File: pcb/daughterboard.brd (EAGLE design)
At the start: 28 x 24 mm, 21 parts, among them IC3 STM32F042F4, SW1 324_SW324_SWITCH_FOOT_HOLE, SW2 324_SW324_SWITCH_FOOT_HOLE, SW3 324_SW, SW4 324_SW, SW5 324_SW324_SWITCH_FOOT_HOLE, SW6 324_SW324_SWITCH_FOOT_HOLE, U2 USBC_16P, U4 XC6206_DEV

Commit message: working on new version
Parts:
- C4: value 1uF -> 100nF
- JP1: device pinhead:2X04 -> pinhead:2X03
- moved C4 5.09 mm to (2.16, 17.9)
- moved JP1 0.55 mm to (10.0, 20.7)
- moved U2 0.38 mm to (5.08, 3.81)
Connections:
- new net N$1: IC3.14, JP1.4
- net +3V3: no longer LED2.A
- net +5V: now also JP1.1
- net GND: now also JP1.2
- net USB_DN: now also IC3.17
- net USB_DP: now also IC3.18
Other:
- board size 28 x 24 mm -> 29 x 24 mm
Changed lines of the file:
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@@
 <setting verticaltext="up"/>
 </settings>
-<grid distance="5" unitdist="mil" unit="mil" style="lines" multiple="1" display="no" altdistance="1" altunitdist="mil" altunit="mil"/>
+<grid distance="5" unitdist="mil" unit="mm" style="lines" multiple="1" display="no" altdistance="1" altunitdist="mil" altunit="mil"/>
 <layers>
 <layer number="1" name="Top" color="4" fill="1" visible="yes" active="yes"/>
@@
 <layer number="43" name="vRestrict" color="2" fill="10" visible="no" active="yes"/>
 <layer number="44" name="Drills" color="7" fill="1" visible="no" active="yes"/>
-<layer number="45" name="Holes" color="7" fill="1" visible="no" active="yes"/>
+<layer number="45" name="Holes" color="7" fill="1" visible="yes" active="yes"/>
 <layer number="46" name="Milling" color="3" fill="1" visible="yes" active="yes"/>
 <layer number="47" name="Measures" color="7" fill="1" visible="no" active="yes"/>
@@
 <plain>
 <wire x1="0" y1="24" x2="0" y2="0" width="0" layer="20"/>
-<wire x1="0" y1="0" x2="28" y2="0" width="0" layer="20"/>
-<wire x1="28" y1="0" x2="28" y2="24" width="0" layer="20"/>
-<wire x1="28" y1="24" x2="0" y2="24" width="0" layer="20"/>
+<wire x1="0" y1="0" x2="29" y2="0" width="0" layer="20"/>
+<wire x1="29" y1="0" x2="29" y2="24" width="0" layer="20"/>
+<wire x1="29" y1="24" x2="0" y2="24" width="0" layer="20"/>
 <text x="69.342" y="33.782" size="0.889" layer="25">SCL</text>
 <text x="66.675" y="33.782" size="0.889" layer="25">SDA</text>
@@
 <text x="68.975" y="21.677" size="1.6764" layer="26" rot="MR180" align="center">git.io/bob_rewind</text>
 <text x="64.135" y="33.782" size="0.889" layer="25">VCC</text>
-<hole x="14" y="2" drill="3"/>
-<circle x="14" y="2" radius="2.6" width="0" layer="41"/>
+<hole x="13" y="2" drill="3"/>
+<circle x="13" y="2" radius="2.6" width="0" layer="41"/>
 <text x="39.925" y="0.68" size="1.778" layer="25" rot="R180" align="center">MOMENTORY
 PSW</text>
@@
 </autorouter>
 <elements>
-<element name="U2" library="my_usbc_16p" package="USBC_16P_FOOT" value="USBC_16P" x="5.461" y="3.81" smashed="yes"/>
+<element name="U2" library="my_usbc_16p" package="USBC_16P_FOOT" value="USBC_16P" x="5.08" y="3.81" smashed="yes"/>
 <element name="R1" library="joyAnalog" package="0805" value="5.1K" x="8.89" y="10.668" smashed="yes" rot="R90">
 <attribute name="NAME" x="28.4218" y="-46.1264" size="0.8128" layer="25" rot="R90"/>
@@
 </element>
 <element name="IC3" library="tx" package="TSSOP20" value="STM32F042F4" x="14.464" y="13.304" smashed="yes" rot="R90"/>
-<element name="C4" library="clock" package="0805@1" value="1uF" x="1.778" y="12.827" smashed="yes">
-<attribute name="NAME" x="53.1622" y="31.5341" size="0.8128" layer="25"/>
+<element name="C4" library="clock" package="0805@1" value="100nF" x="2.159" y="17.907" smashed="yes">
+<attribute name="NAME" x="53.5432" y="36.6141" size="0.8128" layer="25"/>
 </element>
 <element name="SW3" library="3pos_slide_switch_centered" package="342_SWICH_FOOT" value="324_SW" x="21.082" y="9.271" smashed="yes" rot="R90"/>
@@
 <attribute name="NAME" x="62.5564" y="35.0355" size="0.8128" layer="25"/>
 </element>
-<element name="JP1" library="pinhead" library_urn="urn:adsk.eagle:library:325" package="2X04" package3d_urn="urn:adsk.eagle:package:22461/2" value="" x="9.779" y="21.209" smashed="yes">
-<attribute name="POPULARITY" value="47" x="9.779" y="21.209" size="1.778" layer="27" display="off"/>
-<attribute name="VALUE" x="5.969" y="16.764" size="1.27" layer="27"/>
+<element name="JP1" library="pinhead" library_urn="urn:adsk.eagle:library:325" package="2X03" package3d_urn="urn:adsk.eagle:package:22462/2" value="" x="10" y="20.71" locked="yes" smashed="yes">
+<attribute name="POPULARITY" value="62" x="10" y="20.71" locked="yes" size="1.778" layer="27" display="off"/>
+<attribute name="VALUE" x="6.19" y="16.265" locked="yes" size="1.27" layer="27"/>
 </element>
 <element name="SW2" library="3pos_slide_switch" package="342_SWICH_FOOT_HOLE" value="324_SW324_SWITCH_FOOT_HOLE" x="26.289" y="11.43" smashed="yes" rot="R90"/>
@@
 <contactref element="U4" pad="1"/>
 <contactref element="C2" pad="1"/>
-<wire x1="16.038" y1="18.0594" x2="9.7934" y2="27.8638" width="0" layer="19" extent="1-1"/>
+<contactref element="JP1" pad="2"/>
+<wire x1="7.46" y1="21.98" x2="9.7934" y2="27.8638" width="0" layer="19" extent="1-1"/>
 </signal>
 <signal name="+3V3">
@@
 <contactref element="IC3" pad="5"/>
 <contactref element="C4" pad="2"/>
-<contactref element="LED2" pad="A"/>
 <contactref element="SW4" pad="P$1"/>
 <contactref element="SW4" pad="P$4"/>
@@
 <wire x1="8.8392" y1="13.324" x2="11.5462" y2="12.979" width="0" layer="19" extent="1-1"/>
 <wire x1="4.638" y1="12.43" x2="8.8392" y2="13.324" width="0" layer="19" extent="1-1"/>
-<wire x1="2.678" y1="12.827" x2="4.638" y2="12.43" width="0" layer="19" extent="1-1"/>
-<wire x1="3.315" y1="28.032" x2="2.678" y2="12.827" width="0" layer="19" extent="1-1"/>
+<wire x1="3.059" y1="17.907" x2="4.638" y2="12.43" width="0" layer="19" extent="1-1"/>
 </signal>
 <signal name="USB_DP">
 <contactref element="U2" pad="A6"/>
 <contactref element="U2" pad="B6"/>
-<wire x1="6.211" y1="7.6575" x2="5.211" y2="7.6575" width="0" layer="19" extent="1-1"/>
+<contactref element="IC3" pad="18"/>
+<wire x1="5.83" y1="7.6575" x2="11.5462" y2="11.679" width="0" layer="19" extent="1-1"/>
+<wire x1="4.83" y1="7.6575" x2="5.83" y2="7.6575" width="0" layer="19" extent="1-1"/>
 </signal>
 <signal name="N$31">
 <contactref element="R1" pad="1"/>
 <contactref element="U2" pad="B5"/>
-<wire x1="7.211" y1="7.6575" x2="8.89" y2="9.768" width="0" layer="19" extent="1-1"/>
+<wire x1="6.83" y1="7.6575" x2="8.89" y2="9.768" width="0" layer="19" extent="1-1"/>
 </signal>
 <signal name="N$33">
 <contactref element="R2" pad="1"/>
 <contactref element="U2" pad="A5"/>
-<wire x1="4.211" y1="7.6575" x2="2.805" y2="10.287" width="0" layer="19" extent="1-1"/>
+<wire x1="3.83" y1="7.6575" x2="2.805" y2="10.287" width="0" layer="19" extent="1-1"/>
 </signal>
 <signal name="USB_DN">
 <contactref element="U2" pad="A7"/>
 <contactref element="U2" pad="B7"/>
-<wire x1="4.711" y1="7.6575" x2="5.711" y2="7.6575" width="0" layer="19" extent="1-1"/>
+<contactref element="IC3" pad="17"/>
+<wire x1="5.33" y1="7.6575" x2="11.5462" y2="12.329" width="0" layer="19" extent="1-1"/>
+<wire x1="4.33" y1="7.6575" x2="5.33" y2="7.6575" width="0" layer="19" extent="1-1"/>
 </signal>
 <signal name="+5V">
@@
 <contactref element="C1" pad="2"/>
 <contactref element="U4" pad="3"/>
+<contactref element="JP1" pad="1"/>
+<wire x1="4.688" y1="16.129" x2="7.46" y2="19.44" width="0" layer="19" extent="1-1"/>
 <wire x1="5.588" y1="10.43" x2="4.688" y2="16.129" width="0" layer="19" extent="1-1"/>
-<wire x1="7.886" y1="7.6575" x2="5.588" y2="10.43" width="0" layer="19" extent="1-1"/>
-<wire x1="3.036" y1="7.6575" x2="5.588" y2="10.43" width="0" layer="19" extent="1-1"/>
+<wire x1="7.505" y1="7.6575" x2="5.588" y2="10.43" width="0" layer="19" extent="1-1"/>
+<wire x1="2.655" y1="7.6575" x2="5.588" y2="10.43" width="0" layer="19" extent="1-1"/>
 </signal>
 <signal name="BUTTON1">
@@
 <wire x1="5.415" y1="28.032" x2="11.5934" y2="27.8638" width="0" layer="19" extent="1-1"/>
 </signal>
+<signal name="N$1">
+<contactref element="IC3" pad="14"/>
+<contactref element="JP1" pad="4"/>
+<wire x1="11.5462" y1="14.279" x2="10" y2="21.98" width="0" layer="19" extent="1-1"/>
+</signal>
 </signals>

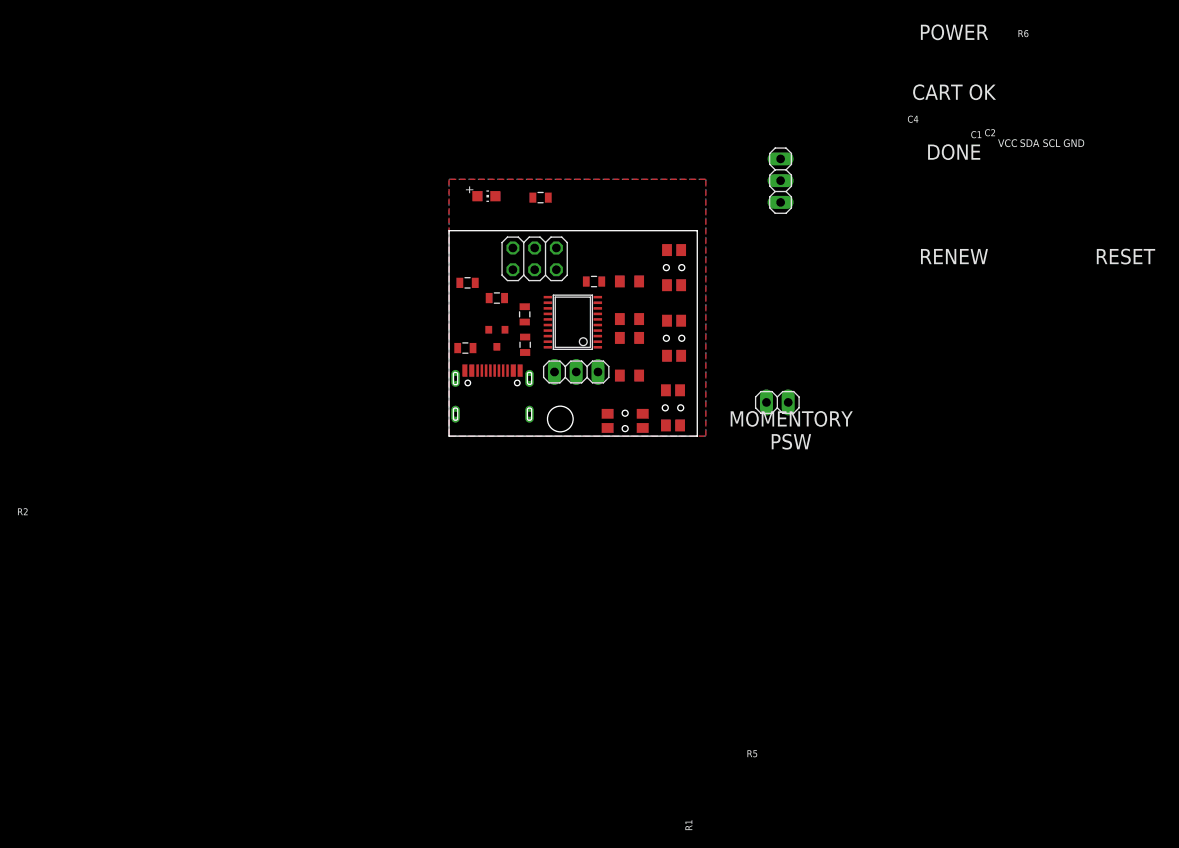
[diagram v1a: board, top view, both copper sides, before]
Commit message: new daughterboard
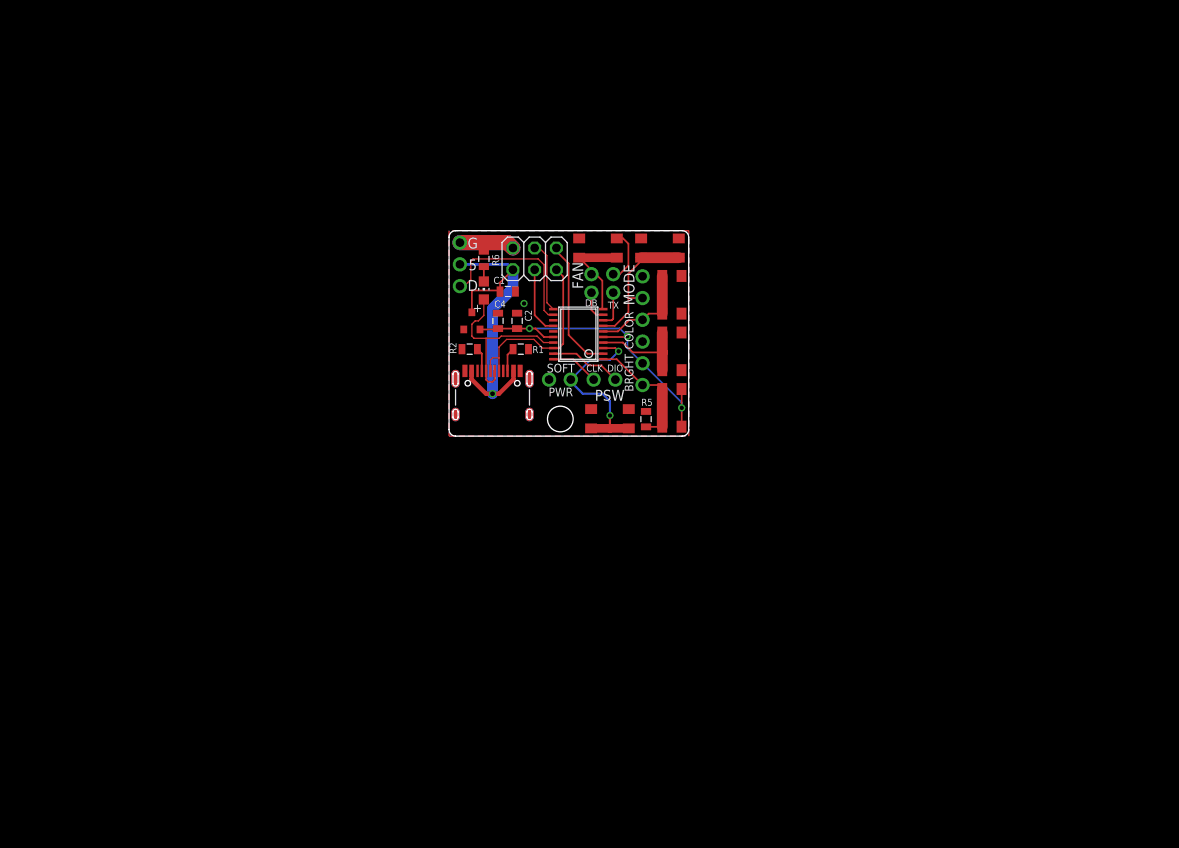
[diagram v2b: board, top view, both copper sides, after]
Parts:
- removed JP2: (no value), pinhead:1X03
- removed JP4: (no value), pinhead:1X02
- removed U2: USBC_16P, my_usbc_16p:USBC_16P_FOOT
- added J4: (no value), SparkFun-Connectors:USB-C-16P
- added U$1, U$2, U$3, U$4, U$5, U$6, U$7: PINHD1X2, adafruit_changed:1X02
- JP3: device pinhead:1X03 -> adafruit_changed:1X03-CLEANBIG
- SW1, SW2, SW5, SW6: value 324_SW324_SWITCH_FOOT_HOLE -> 324_SW; device 3pos_slide_switch:342_SWICH_FOOT_HOLE -> 3pos_slide_switch_centered:342_SWICH_FOOT
- moved SW1 20.6 mm to (17.4, 22.0), turned to 180 degrees
- moved SW6 19.2 mm to (18.8, 2.03), turned to 0 degrees
- moved JP3 18.5 mm to (1.27, 20.1), turned to 90 degrees
- moved R5 17.2 mm to (23.0, 1.99), turned to 270 degrees
- moved SW5 15.7 mm to (26.0, 16.5), turned to 90 degrees
- moved SW4 13.5 mm to (26.0, 3.30)
- moved LED2 11.0 mm to (4.06, 17.0), turned to 0 degrees
- moved SW2 10.7 mm to (24.6, 22.0), turned to 180 degrees
- moved R6 9.76 mm to (4.06, 20.7), turned to 270 degrees
- moved C4 5.69 mm to (5.71, 13.5), turned to 270 degrees
- moved SW3 4.99 mm to (26.0, 9.91)
- moved U4 3.56 mm to (2.67, 13.5), turned to 0 degrees
- moved IC3 1.53 mm to (15.1, 11.9)
- moved C1 1.48 mm to (6.86, 16.9)
- moved C2 1.17 mm to (7.95, 13.5)
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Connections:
- new net N$10: IC3.7, SW2.P$2, SW2.P$3, U$2.1
- new net N$11: IC3.6, SW5.P$2, SW5.P$3, U$3.1
- new net N$12: IC3.3, SW6.P$1, SW6.P$4, U$7.2
- new net N$2: IC3.14, JP1.3
- new net N$3: IC3.19, U$5.2
- new net N$4: IC3.20, U$5.1
- new net N$5: IC3.12, JP3.1
- new net N$6: IC3.2, JP1.6
- new net N$7: IC3.8, U$6.1
- new net N$8: IC3.9, U$6.2
- new net N$9: IC3.10, SW1.P$2, SW1.P$3, U$1.1
- net +3V3: now also U$4.1
- net +5V: now also J4.VBUS1, J4.VBUS2, JP3.2; no longer U2.A4B9, U2.B4A9
- net BUTTON2: now also U$4.2
- net GND: now also J4.GND, J4.GND2, J4.SHLD1, J4.SHLD2, J4.SHLD3, J4.SHLD4, J4.SHLD5, J4.SHLD6, J4.SHLD7, J4.SHLD8, JP3.3, SW1.P$1, SW1.P$4, SW2.P$1, SW2.P$4, SW5.P$1, SW5.P$4, SW6.P$2, SW6.P$3, U$1.2, U$2.2, U$3.2, U$7.1; no longer U2.A1B12, U2.B11A12, U2.P$13, U2.P$14, U2.P$15, U2.P$16
- net N$1: now also IC3.11; no longer IC3.14
- net N$31: now also J4.B5; no longer U2.B5
- net N$33: now also J4.A5; no longer U2.A5
- net USB_DN: now also J4.A7, J4.B7, LED2.A; no longer U2.A7, U2.B7
- net USB_DP: now also J4.A6, J4.B6, JP1.5; no longer U2.A6, U2.B6
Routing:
- net +5V: track 0.00 -> 39.2 mm, vias 0 -> 1
- net +3V3: track 0.00 -> 39.1 mm, vias 0 -> 3
- net USB_DP: track 0.00 -> 22.6 mm
- net N$12: track 0.00 -> 22.2 mm, vias 0 -> 2
- net USB_DN: track 0.00 -> 22.2 mm
- net N$5: track 0.00 -> 19.3 mm
- net GND: track 0.00 -> 19.2 mm, vias 0 -> 1
- net N$10: track 0.00 -> 16.6 mm
- net N$6: track 0.00 -> 15.7 mm
- net BUTTON2: track 0.00 -> 14.6 mm
- net N$11: track 0.00 -> 12.2 mm
- net N$9: track 0.00 -> 11.9 mm
- net BUTTON1: track 0.00 -> 11.8 mm
- net N$3: track 0.00 -> 8.50 mm
- net N$1: track 0.00 -> 8.36 mm
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- added copper zone on layer 16, net GND
- removed copper zone on layer 16, net +3V3
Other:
- board size 29 x 24 mm -> 28 x 24 mm
- board text added: "5"
- board text added: "ATX4VC Expansion Card"
- board text added: "ATX4VC.com dekuNukem"
- board text added: "BRGHT"
- board text added: "COLOR"
- board text added: "D"
- board text added: "DB"
- board text added: "FAN"
- board text added: "MODE"
- board text added: "PSW"
- board text added: "PT1 APR23"
- board text added: "PWR"
- board text added: "SOFT"
- board text removed: "3V3"
- board text removed: "Bob Dishwasher Cassette Rewinder"
- board text removed: "CART OK"
- board text removed: "DONE"
- board text removed: "GND"
- board text removed: "MOMENTORY PSW"
- board text removed: "POWER"
- board text removed: "RENEW"
- board text removed: "RESET"
- board text removed: "RX"
- board text removed: "SCL"
- board text removed: "SDA"
- board text removed: "VCC"
- board text removed: "dekuNukem 2021"
- board text removed: "git.io/bob_rewind"
